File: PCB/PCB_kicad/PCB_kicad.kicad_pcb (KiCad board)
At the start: 2 copper layers, 70 x 70 mm, 21 parts, among them J1 Conn_01x15_Socket, J10 Conn_01x02_Socket, J11 Conn_01x04_Socket, J2 Conn_01x15_Socket, J3 Barrel_Jack_Switch_Pin3Ring, J4 Conn_01x08_Socket, J5 Conn_01x04_Socket, J6 Conn_01x04_Socket, J7 Conn_01x04_Socket, J8 Conn_01x04_Socket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

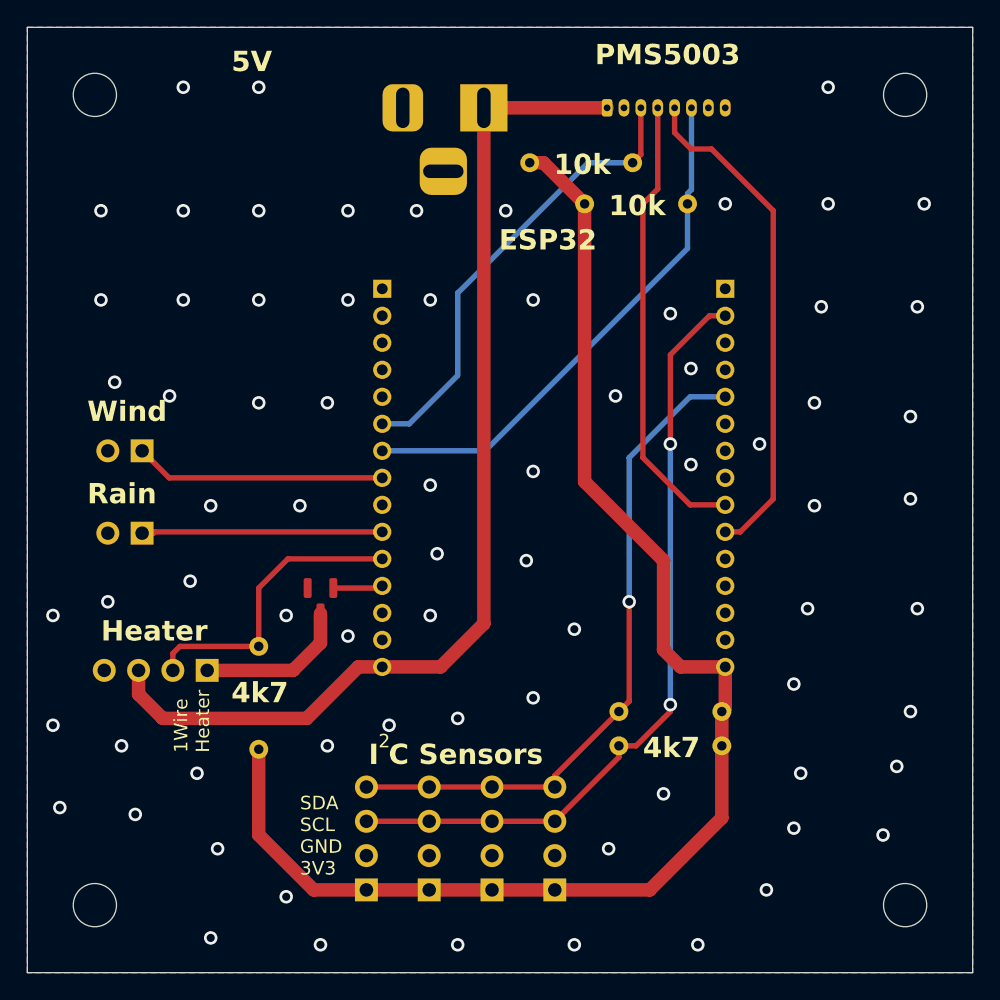
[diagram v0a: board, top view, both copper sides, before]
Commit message: Improved stability
Added some minor tweaks to improve the stability of the desing
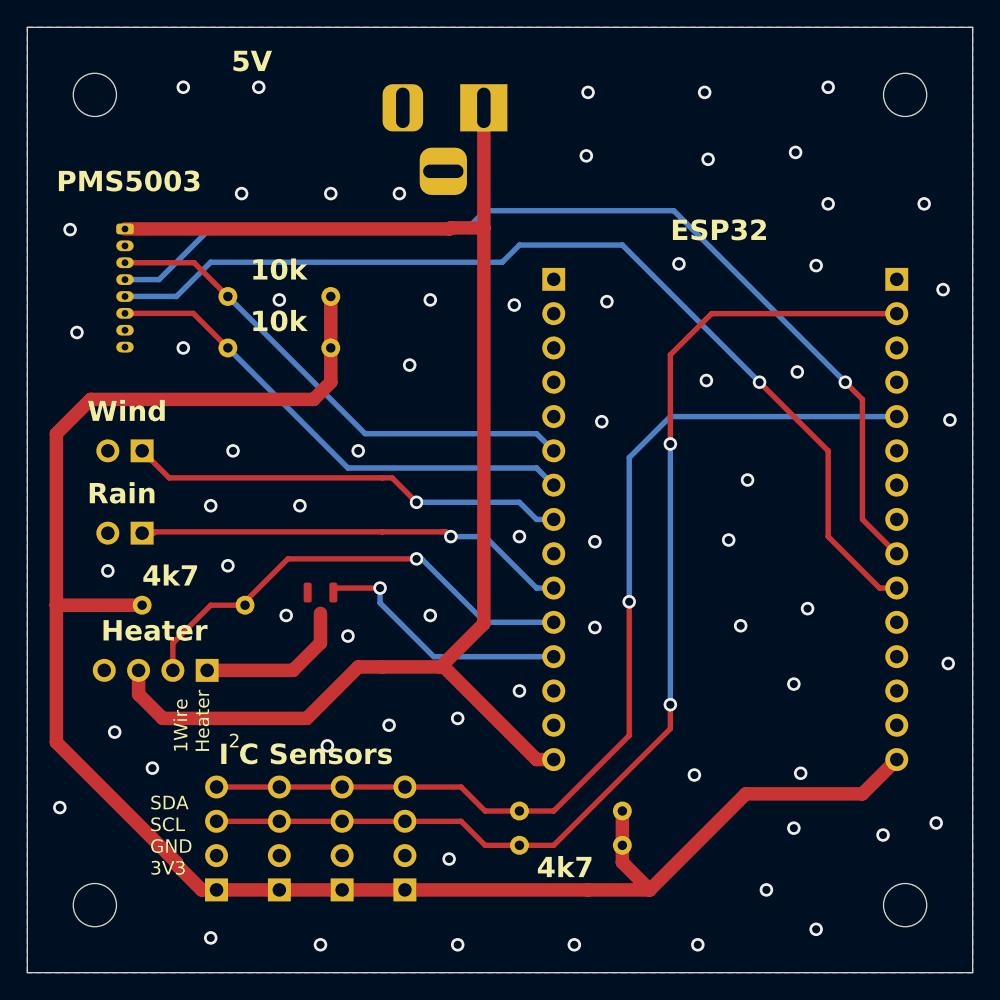
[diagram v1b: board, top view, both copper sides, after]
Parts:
- J1, J2: footprint Connector_PinHeader_2.00mm:PinHeader_1x15_P2.00mm_Vertical -> Connector_PinHeader_2.54mm:PinHeader_1x15_P2.54mm_Vertical
- moved J4 36.8 mm to (62.2, 69.9), turned to -90 degrees
- moved R2 21.6 mm to (77.5, 78.7), turned to 180 degrees
- moved R1 17.8 mm to (77.5, 74.9), turned to 180 degrees
- moved R5 13.7 mm to (63.5, 97.8), turned to 0 degrees
- moved J1 12.7 mm to (94.0, 73.7)
- moved J2 12.7 mm to (119.4, 73.7)
- moved J5 11.1 mm to (83.0, 118.9)
- moved J6 11.1 mm to (78.3, 118.9)
- moved J7 11.1 mm to (73.7, 118.9)
- moved J8 11.1 mm to (69.0, 118.9)
- moved R3 10.4 mm to (99.1, 115.6)
- moved R4 10.4 mm to (99.1, 113.0)
- moved Q1 0.33 mm to (76.7, 97.8)
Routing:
- net /TX2: track 33.9 -> 75.0 mm, vias 0 -> 1
- net /RX2: track 37.4 -> 73.0 mm, vias 0 -> 1
- net +3.3V: track 101.7 -> 135.0 mm
- net +5V: track 78.3 -> 107.0 mm
- net /D21: track 49.6 -> 75.3 mm
- net /D22: track 58.0 -> 83.6 mm
- net /D12: track 3.69 -> 19.1 mm, vias 0 -> 1
- net /D27: track 17.8 -> 32.2 mm, vias 0 -> 1
- net /D25: track 18.6 -> 32.6 mm, vias 0 -> 1
- net /D14: track 22.2 -> 34.6 mm, vias 0 -> 1
- net /D32: track 34.4 -> 37.5 mm
- net /D33: track 39.3 -> 37.0 mm
- net GND: vias 73 -> 66
